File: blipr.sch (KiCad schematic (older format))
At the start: 1 part, among them U1 AY-3-8910

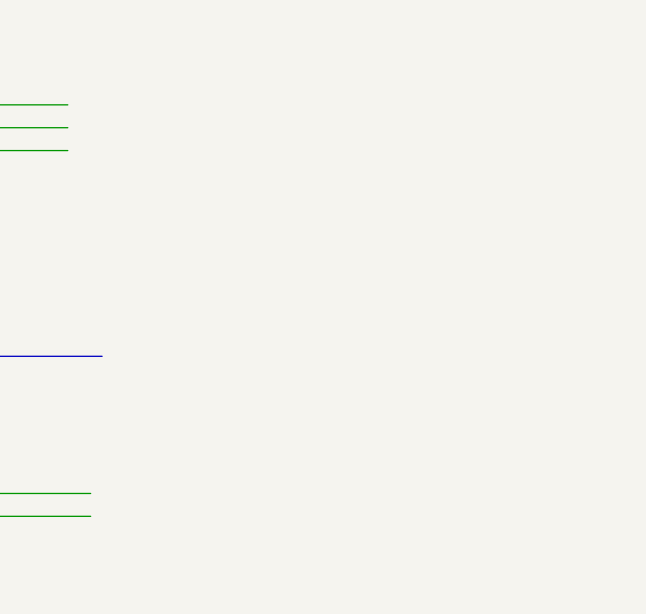
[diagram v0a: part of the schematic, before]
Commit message: lade till en level shifter
precis
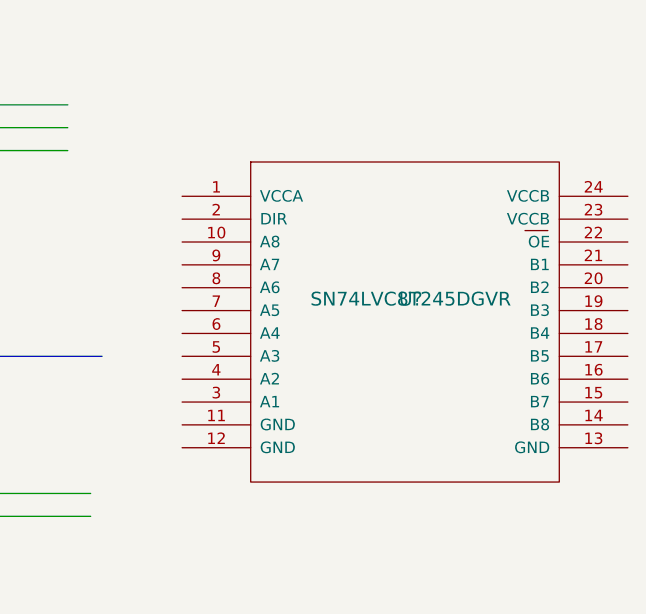
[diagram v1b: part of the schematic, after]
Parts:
- added U?: SN74LVC8T245DGVR, ~, symbol SN74LVC8T245DGVR
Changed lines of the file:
@@
-EESchema Schematic File Version 2  date 24/04/2014 22:05:26
+EESchema Schematic File Version 2
 LIBS:power
 LIBS:device
@@
 Sheet 1 3
 Title ""
-Date "24 apr 2014"
+Date "25 apr 2014"
 Rev ""
 Comp ""
@@
 F4 "Gnd" B R 2950 3800 60
 $EndSheet
+$Comp
+L SN74LVC8T245DGVR U?
+U 1 1 535ADBCA
+P 9650 3750
+F 0 "U?" H 9650 3750 60  0000 C CNN
+F 1 "SN74LVC8T245DGVR" H 9650 3750 60  0000 C CNN
+F 2 "~" H 9650 3750 60  0000 C CNN
+F 3 "~" H 9650 3750 60  0000 C CNN
+	1    9650 3750
+	1    0    0    -1
+$EndComp
 $EndSCHEMATC

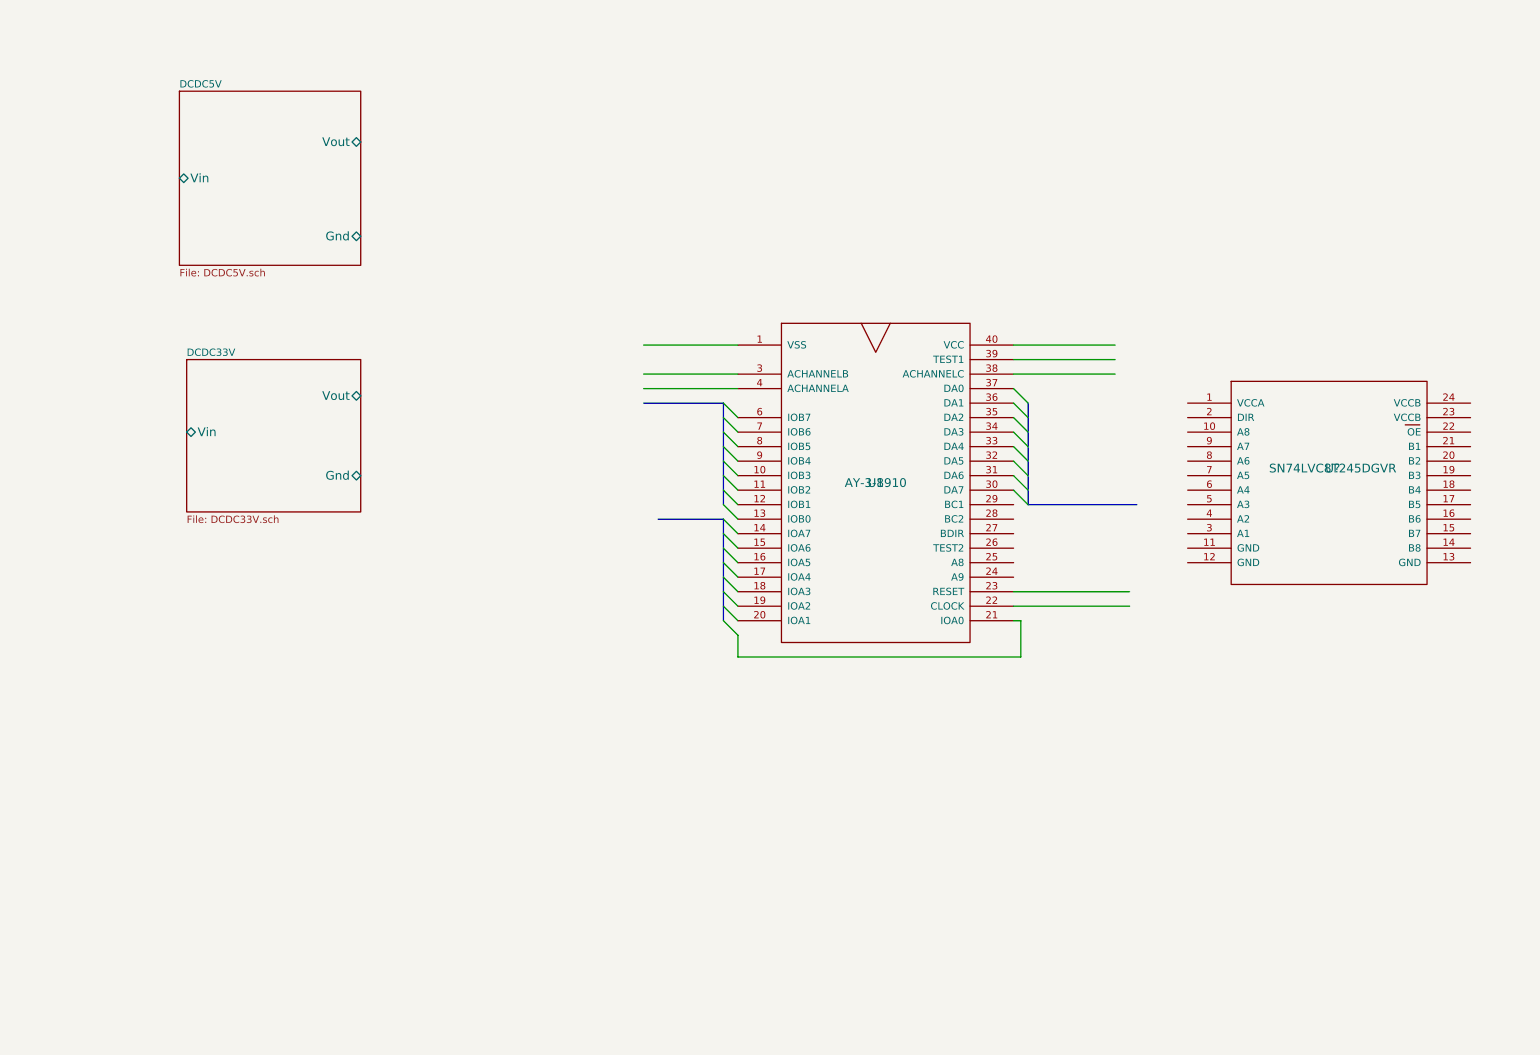
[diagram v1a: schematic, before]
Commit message: added level shifter and bt module
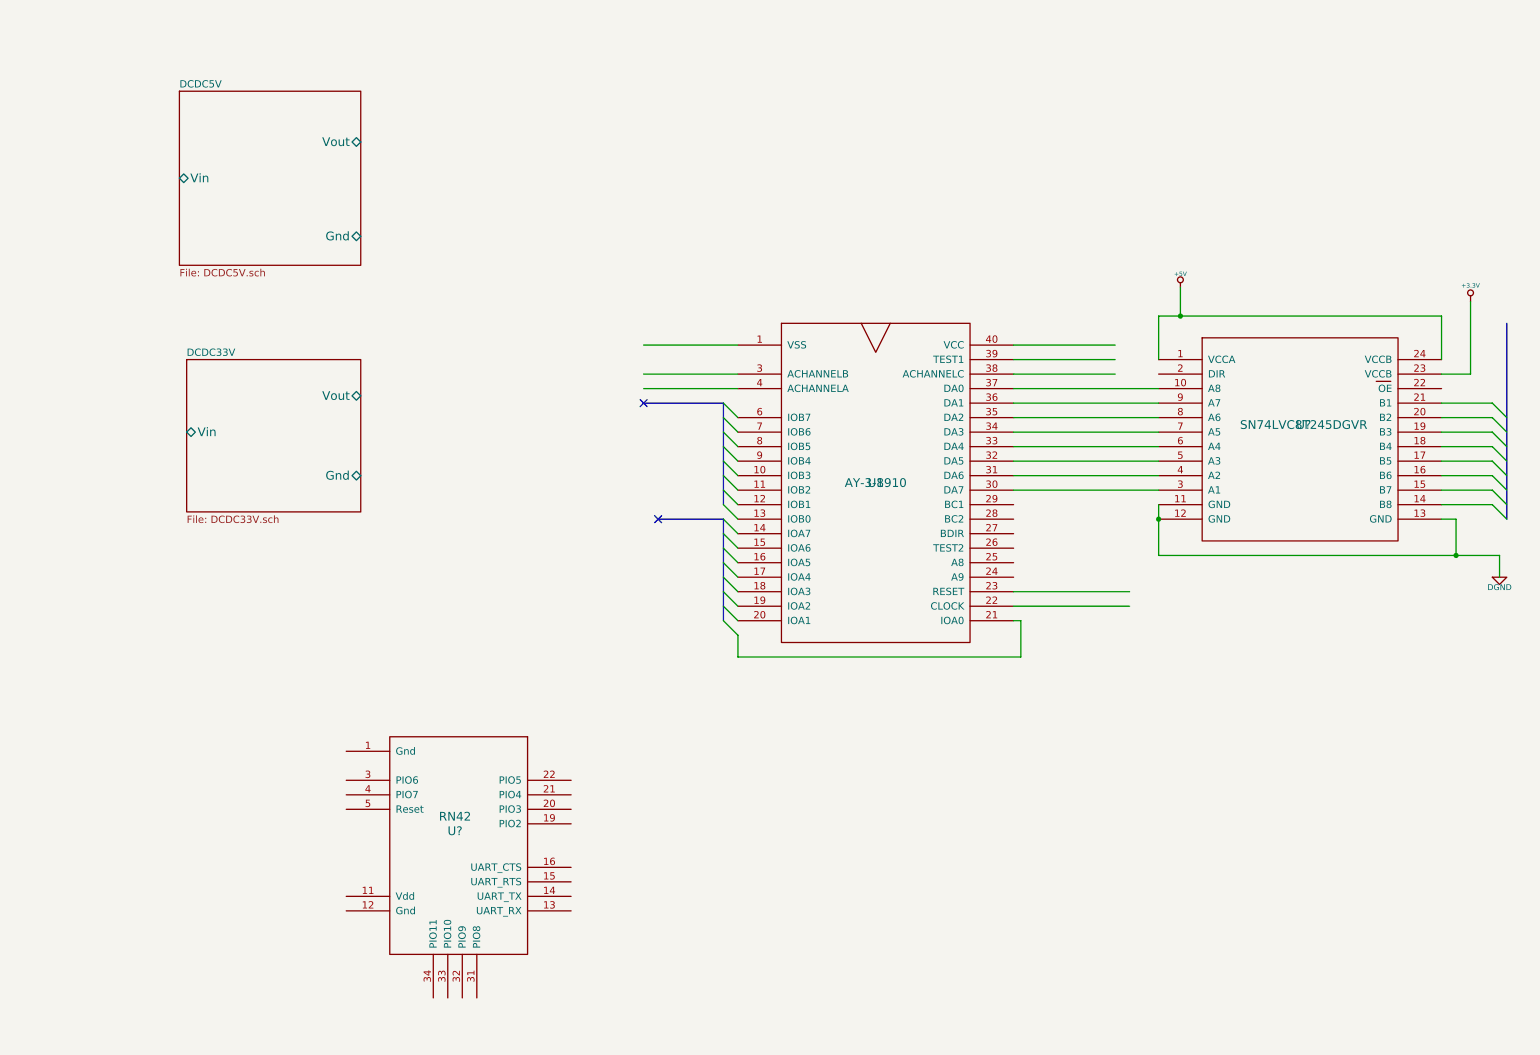
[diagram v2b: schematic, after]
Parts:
- added U?: RN42, ~, symbol RN42
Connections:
- net labels added: +3.3V, +5V, DGND
- wire segments 12 -> 39
- no-connect marks 0 -> 2
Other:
- moved on the sheet: U?
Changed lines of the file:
@@
 	1    0    0    -1
 $EndComp
-Wire Wire Line
-	5550 2900 4900 2900
-Wire Wire Line
-	7450 2900 8150 2900
-Entry Wire Line
-	7450 3500 7550 3600
-Wire Bus Line
-	7550 4000 8300 4000
-Entry Wire Line
-	7450 3400 7550 3500
-Entry Wire Line
-	7450 3300 7550 3400
-Entry Wire Line
-	7450 3200 7550 3300
-Entry Wire Line
-	7450 3600 7550 3700
-Entry Wire Line
-	7450 3700 7550 3800
-Entry Wire Line
-	7450 3800 7550 3900
-Entry Wire Line
-	7450 3900 7550 4000
-Wire Bus Line
-	7550 4000 7550 3300
 Entry Wire Line
 	5450 3400 5550 3500
@@
 Entry Wire Line
 	5450 4700 5550 4800
-Wire Bus Line
-	5450 4100 5450 4800
-Wire Bus Line
-	5450 4100 5000 4100
-Wire Bus Line
-	5450 4000 5450 3300
-Wire Bus Line
-	5450 3300 4900 3300
 Entry Wire Line
 	5450 3300 5550 3400
@@
 Entry Wire Line
 	5450 4400 5550 4500
-Wire Wire Line
-	7450 4600 8250 4600
-Wire Wire Line
-	7450 4700 8250 4700
-Wire Wire Line
-	7450 4800 7500 4800
-Wire Wire Line
-	7500 4800 7500 5050
-Wire Wire Line
-	7500 5050 5550 5050
-Wire Wire Line
-	5550 5050 5550 4900
 Entry Wire Line
 	5450 4800 5550 4900
-Wire Wire Line
-	5550 3100 4900 3100
-Wire Wire Line
-	5550 3200 4900 3200
-Wire Wire Line
-	7450 3000 8150 3000
-Wire Wire Line
-	7450 3100 8150 3100
 $Sheet
 S 1700 1150 1250 1200
@@
 L SN74LVC8T245DGVR U?
 U 1 1 535ADBCA
-P 9650 3750
-F 0 "U?" H 9650 3750 60  0000 C CNN
-F 1 "SN74LVC8T245DGVR" H 9650 3750 60  0000 C CNN
-F 2 "~" H 9650 3750 60  0000 C CNN
-F 3 "~" H 9650 3750 60  0000 C CNN
-	1    9650 3750
-	1    0    0    -1
-$EndComp
+P 9450 3450
+F 0 "U?" H 9450 3450 60  0000 C CNN
+F 1 "SN74LVC8T245DGVR" H 9450 3450 60  0000 C CNN
+F 2 "~" H 9450 3450 60  0000 C CNN
+F 3 "~" H 9450 3450 60  0000 C CNN
+	1    9450 3450
+	1    0    0    -1
+$EndComp
+NoConn ~ 4900 3300
+NoConn ~ 5000 4100
+Wire Wire Line
+	5550 2900 4900 2900
+Wire Wire Line
+	7450 2900 8150 2900
+Wire Bus Line
+	5450 4100 5450 4800
+Wire Bus Line
+	5450 4100 5000 4100
+Wire Bus Line
+	5450 4000 5450 3300
+Wire Bus Line
+	5450 3300 4900 3300
+Wire Wire Line
+	7450 4600 8250 4600
+Wire Wire Line
+	7450 4700 8250 4700
+Wire Wire Line
+	7450 4800 7500 4800
+Wire Wire Line
+	7500 4800 7500 5050
+Wire Wire Line
+	7500 5050 5550 5050
+Wire Wire Line
+	5550 5050 5550 4900
+Wire Wire Line
+	5550 3100 4900 3100
+Wire Wire Line
+	5550 3200 4900 3200
+Wire Wire Line
+	7450 3000 8150 3000
+Wire Wire Line
+	7450 3100 8150 3100
+Wire Wire Line
+	7450 3200 8450 3200
+Wire Wire Line
+	7450 3300 8450 3300
+Wire Wire Line
+	7450 3400 8450 3400
+Wire Wire Line
+	7450 3500 8450 3500
+Wire Wire Line
+	7450 3600 8450 3600
+Wire Wire Line
+	7450 3700 8450 3700
+Wire Wire Line
+	7450 3800 8450 3800
+Wire Wire Line
+	7450 3900 8450 3900
+Wire Wire Line
+	8450 4000 8450 4350
+Wire Wire Line
+	8450 4350 10800 4350
+Wire Wire Line
+	10500 4350 10500 4100
+Wire Wire Line
+	10500 4100 10400 4100
+Connection ~ 8450 4100
+Connection ~ 10500 4350
+Wire Wire Line
+	10400 3300 10750 3300
+Wire Wire Line
+	10400 3400 10750 3400
+Wire Wire Line
+	10400 3500 10750 3500
+Wire Wire Line
+	10400 3600 10750 3600
+Wire Wire Line
+	10400 3700 10750 3700
+Wire Wire Line
+	10400 3800 10750 3800
+Wire Wire Line
+	10400 3900 10750 3900
+Wire Wire Line
+	10400 4000 10750 4000
+Wire Bus Line
+	10850 4100 10850 2750
+Entry Wire Line
+	10750 3300 10850 3400
+Entry Wire Line
+	10750 3400 10850 3500
+Entry Wire Line
+	10750 3500 10850 3600
+Entry Wire Line
+	10750 3600 10850 3700
+Entry Wire Line
+	10750 3700 10850 3800
+Entry Wire Line
+	10750 3800 10850 3900
+Entry Wire Line
+	10750 3900 10850 4000
+Entry Wire Line
+	10750 4000 10850 4100
+Wire Wire Line
+	10400 3000 10400 2700
+Wire Wire Line
+	10400 2700 8450 2700
+Wire Wire Line
+	8450 2700 8450 3000
+Wire Wire Line
+	8600 2700 8600 2500
+Connection ~ 8600 2700
+Wire Wire Line
+	10800 4350 10800 4500
+$Comp
+L DGND #PWR?
+U 1 1 535AFAC2
+P 10800 4500
+F 0 "#PWR?" H 10800 4500 40  0001 C CNN
+F 1 "DGND" H 10800 4430 40  0000 C CNN
+F 2 "" H 10800 4500 60  0000 C CNN
+F 3 "" H 10800 4500 60  0000 C CNN
+	1    10800 4500
+	1    0    0    -1
+$EndComp
+$Comp
+L +5V #PWR?
+U 1 1 535B0C08
+P 8600 2500
+F 0 "#PWR?" H 8600 2590 20  0001 C CNN
+F 1 "+5V" H 8600 2590 30  0000 C CNN
+F 2 "" H 8600 2500 60  0000 C CNN
+F 3 "" H 8600 2500 60  0000 C CNN
+	1    8600 2500
+	1    0    0    -1
+$EndComp
+Wire Wire Line
+	10400 3100 10600 3100
+Wire Wire Line
+	10600 3100 10600 2600
+$Comp
+L +3.3V #PWR?
+U 1 1 535B0CC5
+P 10600 2600
+F 0 "#PWR?" H 10600 2560 30  0001 C CNN
+F 1 "+3.3V" H 10600 2710 30  0000 C CNN
+F 2 "" H 10600 2600 60  0000 C CNN
+F 3 "" H 10600 2600 60  0000 C CNN
+	1    10600 2600
+	1    0    0    -1
+$EndComp
+$Comp
+L RN42 U?
+U 1 1 535B0DBE
+P 3600 6150
+F 0 "U?" H 3600 6050 60  0000 C CNN
+F 1 "RN42" H 3600 6150 60  0000 C CNN
+F 2 "~" H 3600 6150 60  0000 C CNN
+F 3 "~" H 3600 6150 60  0000 C CNN
+	1    3600 6150
+	1    0    0    -1
+$EndComp

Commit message: f
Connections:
- net labels added: +12V
- wire segments 39 -> 57
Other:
- moved on the sheet: U1, U?

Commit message: Layout 0.01
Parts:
- gave numbers to parts that had none: 2
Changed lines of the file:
@@
-EESchema Schematic File Version 2
+EESchema Schematic File Version 2  date 26/04/2014 12:34:29
 LIBS:power
 LIBS:device
@@
 Sheet 1 3
 Title ""
-Date "25 apr 2014"
+Date "26 apr 2014"
 Rev ""
 Comp ""
@@
 $EndSheet
 $Comp
-L SN74LVC8T245DGVR U?
+L SN74LVC8T245DGVR U5
 U 1 1 535ADBCA
 P 8350 2500
-F 0 "U?" H 8350 2500 60  0000 C CNN
+F 0 "U5" H 8350 2500 60  0000 C CNN
 F 1 "SN74LVC8T245DGVR" H 8350 2500 60  0000 C CNN
 F 2 "~" H 8350 2500 60  0000 C CNN
@@
 	9700 3400 9700 3550
 $Comp
-L DGND #PWR?
+L DGND #PWR8
 U 1 1 535AFAC2
 P 9700 3550
-F 0 "#PWR?" H 9700 3550 40  0001 C CNN
+F 0 "#PWR8" H 9700 3550 40  0001 C CNN
 F 1 "DGND" H 9700 3480 40  0000 C CNN
 F 2 "" H 9700 3550 60  0000 C CNN
@@
 $EndComp
 $Comp
-L +5V #PWR?
+L +5V #PWR5
 U 1 1 535B0C08
 P 7500 1550
-F 0 "#PWR?" H 7500 1640 20  0001 C CNN
+F 0 "#PWR5" H 7500 1640 20  0001 C CNN
 F 1 "+5V" H 7500 1640 30  0000 C CNN
 F 2 "" H 7500 1550 60  0000 C CNN
@@
 	9500 2150 9500 1650
 $Comp
-L +3.3V #PWR?
+L +3.3V #PWR6
 U 1 1 535B0CC5
 P 9500 1650
-F 0 "#PWR?" H 9500 1610 30  0001 C CNN
+F 0 "#PWR6" H 9500 1610 30  0001 C CNN
 F 1 "+3.3V" H 9500 1760 30  0000 C CNN
 F 2 "" H 9500 1650 60  0000 C CNN
@@
 $EndComp
 $Comp
-L RN42 U?
+L RN42 U4
 U 1 1 535B0DBE
 P 3600 6150
-F 0 "U?" H 3600 6050 60  0000 C CNN
+F 0 "U4" H 3600 6050 60  0000 C CNN
 F 1 "RN42" H 3600 6150 60  0000 C CNN
 F 2 "~" H 3600 6150 60  0000 C CNN
@@
 	7350 2150 7200 2150
 $Comp
-L DGND #PWR?
+L DGND #PWR7
 U 1 1 535AD1D8
 P 9600 4150
-F 0 "#PWR?" H 9600 4150 40  0001 C CNN
+F 0 "#PWR7" H 9600 4150 40  0001 C CNN
 F 1 "DGND" H 9600 4080 40  0000 C CNN
 F 2 "" H 9600 4150 60  0000 C CNN
@@
 Connection ~ 1100 1750
 $Comp
-L DGND #PWR?
+L DGND #PWR4
 U 1 1 535AD824
 P 3450 4350
-F 0 "#PWR?" H 3450 4350 40  0001 C CNN
+F 0 "#PWR4" H 3450 4350 40  0001 C CNN
 F 1 "DGND" H 3450 4280 40  0000 C CNN
 F 2 "" H 3450 4350 60  0000 C CNN
@@
 $EndComp
 $Comp
-L +3.3V #PWR?
+L +3.3V #PWR2
 U 1 1 535AD87B
 P 3100 2900
-F 0 "#PWR?" H 3100 2860 30  0001 C CNN
+F 0 "#PWR2" H 3100 2860 30  0001 C CNN
 F 1 "+3.3V" H 3100 3010 30  0000 C CNN
 F 2 "" H 3100 2900 60  0000 C CNN
@@
 $EndComp
 $Comp
-L +5V #PWR?
+L +5V #PWR3
 U 1 1 535AD88A
 P 3150 900
-F 0 "#PWR?" H 3150 990 20  0001 C CNN
+F 0 "#PWR3" H 3150 990 20  0001 C CNN
 F 1 "+5V" H 3150 990 30  0000 C CNN
 F 2 "" H 3150 900 60  0000 C CNN
@@
 $EndComp
 $Comp
-L +12V #PWR?
+L +12V #PWR1
 U 1 1 535AD899
 P 1100 1450
-F 0 "#PWR?" H 1100 1400 20  0001 C CNN
+F 0 "#PWR1" H 1100 1400 20  0001 C CNN
 F 1 "+12V" H 1100 1550 30  0000 C CNN
 F 2 "" H 1100 1450 60  0000 C CNN

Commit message: Layout 0.02
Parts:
- added K1: CONN_3, symbol CONN_3
- added P1: CONN_3X2, symbol CONN_3X2
- added U6: FT231XS, ~, symbol FT231XS
- added U7: ATXMEGA8E5, ~, symbol ATXMEGA8E5
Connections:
- wire segments 57 -> 61
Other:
- moved on the sheet: U4
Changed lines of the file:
@@
-EESchema Schematic File Version 2  date 26/04/2014 12:34:29
+EESchema Schematic File Version 2  date 26/04/2014 16:22:01
 LIBS:power
 LIBS:device
@@
 	6350 2050 7050 2050
 Wire Wire Line
-	6350 2250 7350 2250
-Wire Wire Line
-	6350 2350 7350 2350
-Wire Wire Line
-	6350 2450 7350 2450
-Wire Wire Line
-	6350 2550 7350 2550
-Wire Wire Line
-	6350 2650 7350 2650
-Wire Wire Line
-	6350 2750 7350 2750
-Wire Wire Line
-	6350 2850 7350 2850
-Wire Wire Line
-	6350 2950 7350 2950
-Wire Wire Line
 	7350 3050 7350 3400
 Wire Wire Line
@@
 	9700 3400 9700 3550
 $Comp
-L DGND #PWR8
+L DGND #PWR01
 U 1 1 535AFAC2
 P 9700 3550
-F 0 "#PWR8" H 9700 3550 40  0001 C CNN
+F 0 "#PWR01" H 9700 3550 40  0001 C CNN
 F 1 "DGND" H 9700 3480 40  0000 C CNN
 F 2 "" H 9700 3550 60  0000 C CNN
@@
 $EndComp
 $Comp
-L +5V #PWR5
+L +5V #PWR02
 U 1 1 535B0C08
 P 7500 1550
-F 0 "#PWR5" H 7500 1640 20  0001 C CNN
+F 0 "#PWR02" H 7500 1640 20  0001 C CNN
 F 1 "+5V" H 7500 1640 30  0000 C CNN
 F 2 "" H 7500 1550 60  0000 C CNN
@@
 	9500 2150 9500 1650
 $Comp
-L +3.3V #PWR6
+L +3.3V #PWR03
 U 1 1 535B0CC5
 P 9500 1650
-F 0 "#PWR6" H 9500 1610 30  0001 C CNN
+F 0 "#PWR03" H 9500 1610 30  0001 C CNN
 F 1 "+3.3V" H 9500 1760 30  0000 C CNN
 F 2 "" H 9500 1650 60  0000 C CNN
@@
 L RN42 U4
 U 1 1 535B0DBE
-P 3600 6150
-F 0 "U4" H 3600 6050 60  0000 C CNN
-F 1 "RN42" H 3600 6150 60  0000 C CNN
-F 2 "~" H 3600 6150 60  0000 C CNN
-F 3 "~" H 3600 6150 60  0000 C CNN
-	1    3600 6150
+P 9650 5450
+F 0 "U4" H 9650 5350 60  0000 C CNN
+F 1 "RN42" H 9650 5450 60  0000 C CNN
+F 2 "~" H 9650 5450 60  0000 C CNN
+F 3 "~" H 9650 5450 60  0000 C CNN
+	1    9650 5450
 	1    0    0    -1
 $EndComp
@@
 	7350 2150 7200 2150
 $Comp
-L DGND #PWR7
+L DGND #PWR04
 U 1 1 535AD1D8
 P 9600 4150
-F 0 "#PWR7" H 9600 4150 40  0001 C CNN
+F 0 "#PWR04" H 9600 4150 40  0001 C CNN
 F 1 "DGND" H 9600 4080 40  0000 C CNN
 F 2 "" H 9600 4150 60  0000 C CNN
@@
 Connection ~ 1100 1750
 $Comp
-L DGND #PWR4
+L DGND #PWR05
 U 1 1 535AD824
 P 3450 4350
-F 0 "#PWR4" H 3450 4350 40  0001 C CNN
+F 0 "#PWR05" H 3450 4350 40  0001 C CNN
 F 1 "DGND" H 3450 4280 40  0000 C CNN
 F 2 "" H 3450 4350 60  0000 C CNN
@@
 $EndComp
 $Comp
-L +3.3V #PWR2
+L +3.3V #PWR06
 U 1 1 535AD87B
 P 3100 2900
-F 0 "#PWR2" H 3100 2860 30  0001 C CNN
+F 0 "#PWR06" H 3100 2860 30  0001 C CNN
 F 1 "+3.3V" H 3100 3010 30  0000 C CNN
 F 2 "" H 3100 2900 60  0000 C CNN
@@
 $EndComp
 $Comp
-L +5V #PWR3
+L +5V #PWR07
 U 1 1 535AD88A
 P 3150 900
-F 0 "#PWR3" H 3150 990 20  0001 C CNN
+F 0 "#PWR07" H 3150 990 20  0001 C CNN
 F 1 "+5V" H 3150 990 30  0000 C CNN
 F 2 "" H 3150 900 60  0000 C CNN
@@
 $EndComp
 $Comp
-L +12V #PWR1
+L +12V #PWR08
 U 1 1 535AD899
 P 1100 1450
-F 0 "#PWR1" H 1100 1400 20  0001 C CNN
+F 0 "#PWR08" H 1100 1400 20  0001 C CNN
 F 1 "+12V" H 1100 1550 30  0000 C CNN
 F 2 "" H 1100 1450 60  0000 C CNN
@@
 Wire Wire Line
 	6600 2150 6600 1600
+$Comp
+L FT231XS U6
+U 1 1 535BA9DD
+P 2800 6100
+F 0 "U6" H 2800 6100 60  0000 C CNN
+F 1 "FT231XS" H 2800 6100 60  0000 C CNN
+F 2 "~" H 2800 6100 60  0000 C CNN
+F 3 "~" H 2800 6100 60  0000 C CNN
+	1    2800 6100
+	1    0    0    -1
+$EndComp
+$Comp
+L ATXMEGA8E5 U7
+U 1 1 535BB5A6
+P 5750 6050
+F 0 "U7" H 5750 5950 60  0000 C CNN
+F 1 "ATXMEGA8E5" H 5750 6050 60  0000 C CNN
+F 2 "~" H 5750 6050 60  0000 C CNN
+F 3 "~" H 5750 6050 60  0000 C CNN
+	1    5750 6050
+	1    0    0    -1
+$EndComp
+$Comp
+L CONN_3 K1
+U 1 1 535BB85F
+P 1000 750
+F 0 "K1" V 950 750 50  0000 C CNN
+F 1 "CONN_3" V 1050 750 40  0000 C CNN
+F 2 "" H 1000 750 60  0000 C CNN
+F 3 "" H 1000 750 60  0000 C CNN
+	1    1000 750
+	0    -1   -1   0
+$EndComp
+$Comp
+L CONN_3X2 P1
+U 1 1 535BB910
+P 7800 6550
+F 0 "P1" H 7800 6800 50  0000 C CNN
+F 1 "CONN_3X2" V 7800 6600 40  0000 C CNN
+F 2 "" H 7800 6550 60  0000 C CNN
+F 3 "" H 7800 6550 60  0000 C CNN
+	1    7800 6550
+	1    0    0    -1
+$EndComp
+Wire Wire Line
+	6350 2950 6600 2950
+Wire Wire Line
+	6600 2950 6600 2250
+Wire Wire Line
+	6600 2250 7350 2250
+Wire Wire Line
+	7350 2350 6650 2350
+Wire Wire Line
+	6650 2350 6650 2850
+Wire Wire Line
+	6650 2850 6350 2850
+Wire Wire Line
+	6700 2750 6350 2750
+Wire Wire Line
+	6700 2450 7350 2450
+Wire Wire Line
+	7350 2550 6750 2550
+Wire Wire Line
+	6750 2550 6750 2650
+Wire Wire Line
+	6750 2650 6350 2650
+Wire Wire Line
+	6700 2450 6700 2750
 $EndSCHEMATC

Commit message: Layout 0.03
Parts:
- added C5, C6: 47p, ~, symbol C
- added C7: 100n, ~, symbol C
- added CON1: BARREL_JACK, symbol BARREL_JACK
- added D3, D4: LED, ~, symbol LED
- added P2: CONN_6, symbol CONN_6
- added R1, R2: 27, ~, symbol R
- added R3, R4: 330, ~, symbol R
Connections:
- net labels added: BLIP0, BLIP1, BLIP2, BLIP3, BLIP4, BLIP5, BLIP6, BLIP7, CTS, FGND, PDI_CLK, PDI_DATA, PIO2, PIO5, RTS, RX, TX
- wire segments 61 -> 124
- no-connect marks 2 -> 4
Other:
- moved on the sheet: K1, P1, U4, U6, U7
